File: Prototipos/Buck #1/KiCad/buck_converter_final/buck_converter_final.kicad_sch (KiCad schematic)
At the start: 25 parts, among them J1 Conn_01x03_Pin, J2 Screw_Terminal_01x02, J3 Screw_Terminal_01x02, Q1 IRF9540NPBF, Q3 NPN

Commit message: Primera versión PCB final Buck
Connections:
- net AGND: now also J1.2 (Pin_2); no longer J1.3 (Pin_3)
- net RETRO_MICRO: now also J1.3 (Pin_3); no longer J1.2 (Pin_2)
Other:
- company: (none) -> Alesandria - Cignetti - Galliano
- title: (none) -> PCB final Convertidor Buck
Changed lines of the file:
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@@
 	(generator_version "9.0")
 	(paper "A4")
+	(title_block
+		(title "PCB final Convertidor Buck")
+		(company "Alesandria - Cignetti - Galliano")
+	)
 	(rectangle
 		(start 130.81 85.09)
@@
 	(wire
 		(pts
+			(xy 81.28 38.1) (xy 101.6 38.1)
+		)
+		(stroke
+			(width 0)
+			(type default)
+		)
+	)
+	(wire
+		(pts
 			(xy 102.87 81.28) (xy 133.35 81.28)
 		)
@@
 	(wire
 		(pts
-			(xy 81.28 38.1) (xy 83.82 38.1)
-		)
-		(stroke
-			(width 0)
-			(type default)
-		)
-	)
-	(wire
-		(pts
 			(xy 133.35 81.28) (xy 149.86 81.28)
 		)
@@
 	(wire
 		(pts
-			(xy 81.28 40.64) (xy 83.82 40.64)
-		)
-		(stroke
-			(width 0)
-			(type default)
-		)
-	)
-	(wire
-		(pts
 			(xy 138.43 64.77) (xy 138.43 69.85)
 		)
@@
 	(wire
 		(pts
+			(xy 83.82 40.64) (xy 81.28 40.64)
+		)
+		(stroke
+			(width 0)
+			(type default)
+		)
+	)
+	(wire
+		(pts
 			(xy 118.11 41.91) (xy 123.19 41.91)
 		)
@@
 	(wire
 		(pts
-			(xy 83.82 40.64) (xy 83.82 41.91)
-		)
-		(stroke
-			(width 0)
-			(type default)
-		)
-	)
-	(wire
-		(pts
 			(xy 156.21 87.63) (xy 156.21 90.17)
 		)
@@
 		(pts
 			(xy 181.61 96.52) (xy 181.61 95.25)
+		)
+		(stroke
+			(width 0)
+			(type default)
+		)
+	)
+	(wire
+		(pts
+			(xy 101.6 38.1) (xy 101.6 39.37)
 		)
 		(stroke
@@
 	(global_label "RETRO_MICRO"
 		(shape input)
-		(at 83.82 38.1 0)
+		(at 83.82 40.64 0)
 		(fields_autoplaced yes)
 		(effects
@@
 		)
 		(property "Intersheetrefs" "${INTERSHEET_REFS}"
-			(at 99.6866 38.1 0)
+			(at 99.6866 40.64 0)
 			(effects
 				(font
@@
 	(symbol
 		(lib_id "power:GND")
-		(at 83.82 41.91 0)
+		(at 101.6 39.37 0)
 		(unit 1)
 		(exclude_from_sim no)
@@
 		(dnp no)
 		(property "Reference" "#PWR01"
-			(at 83.82 48.26 0)
+			(at 101.6 45.72 0)
 			(effects
 				(font
@@
 		)
 		(property "Value" "AGND"
-			(at 83.82 45.466 0)
+			(at 101.6 42.926 0)
 			(effects
 				(font
@@
 		)
 		(property "Footprint" ""
-			(at 83.82 41.91 0)
+			(at 101.6 39.37 0)
 			(effects
 				(font
@@
 		)
 		(property "Datasheet" ""
-			(at 83.82 41.91 0)
+			(at 101.6 39.37 0)
 			(effects
 				(font
@@
 		)
 		(property "Description" "Power symbol creates a global label with name \"GND\" , ground"
-			(at 83.82 41.91 0)
-			(effects
-				(font
+			(at 101.6 39.37 0)
+			(effects
+				(font

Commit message: Mejoras en PCB
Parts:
- R11: value 33k -> 2.2k
- R13: value 1k -> 100k
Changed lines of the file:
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@@
 			)
 		)
-		(property "Value" "1k"
+		(property "Value" "100k"
 			(at 158.242 111.76 0)
 			(effects
@@
 			)
 		)
-		(property "Value" "33k"
+		(property "Value" "2.2k"
 			(at 152.4 105.918 90)
 			(effects

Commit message: Avances PCB convertidor Buck
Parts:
- removed J1: Conn_01x03_Pin, Connector_PinHeader_2.54mm:PinHeader_1x03_P2.54mm_Vertical, symbol Connector:Conn_01x03_Pin
- removed J2: Screw_Terminal_01x02, TerminalBlock_Phoenix:TerminalBlock_Phoenix_MKDS-1,5-2-5.08_1x02_P5.08mm_Horizontal, symbol Connector:Screw_Terminal_01x02
- added J4: ~, Proyecto_Final:BUS_PCIE_x4_NSH, symbol Proyecto_Final:PCIE_x4_NSH
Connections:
- net 12V: now also J4.4 (12Vdc)
- net AGND: now also J4.40 (AGND)
- net PGND: now also J4.2 (PGND)
- net PWM_CONTROL: now also J4.8 (S2)
- net RETRO_MICRO: now also J4.10 (S4)

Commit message: Avances en PCB final buck, versión 1.1
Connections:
- net PWM_CONTROL: now also J4.26 (S20); no longer J4.8 (S2)
- net RETRO_MICRO: now also J4.8 (S2); no longer J4.10 (S4)
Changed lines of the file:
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@@
+	(wire
+		(pts
+			(xy 257.81 71.12) (xy 254 71.12)
+		)
+		(stroke
+			(width 0)
+			(type default)
+		)
+	)
 	(wire
 		(pts
@@
 	(wire
 		(pts
-			(xy 254 50.8) (xy 256.54 50.8)
-		)
-		(stroke
-			(width 0)
-			(type default)
-		)
-	)
-	(wire
-		(pts
 			(xy 149.86 71.12) (xy 149.86 81.28)
 		)
@@
 	(wire
 		(pts
-			(xy 254 48.26) (xy 256.54 48.26)
-		)
-		(stroke
-			(width 0)
-			(type default)
-		)
-	)
-	(wire
-		(pts
 			(xy 167.64 88.9) (xy 166.37 88.9)
+		)
+		(stroke
+			(width 0)
+			(type default)
+		)
+	)
+	(wire
+		(pts
+			(xy 256.54 48.26) (xy 254 48.26)
 		)
 		(stroke
@@
 	(global_label "PWM_CONTROL"
 		(shape output)
-		(at 256.54 48.26 0)
+		(at 257.81 71.12 0)
 		(fields_autoplaced yes)
 		(effects
@@
 		)
 		(property "Intersheetrefs" "${INTERSHEET_REFS}"
-			(at 273.1928 48.26 0)
+			(at 274.4628 71.12 0)
 			(effects
 				(font
@@
 	(global_label "RETRO_MICRO"
 		(shape input)
-		(at 256.54 50.8 0)
+		(at 256.54 48.26 0)
 		(fields_autoplaced yes)
 		(effects
@@
 		)
 		(property "Intersheetrefs" "${INTERSHEET_REFS}"
-			(at 272.4066 50.8 0)
-			(effects
-				(font
+			(at 272.4066 48.26 0)
+			(effects
+				(font

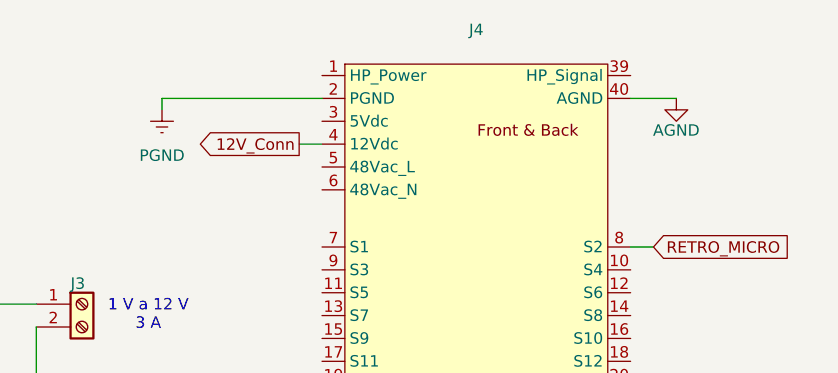
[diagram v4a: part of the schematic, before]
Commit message: Agregado pin HP
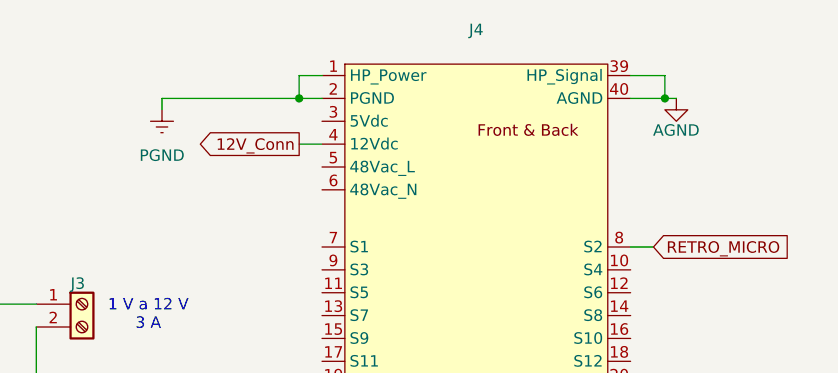
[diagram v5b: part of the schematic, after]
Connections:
- net AGND: now also J4.39 (HP_Signal)
- net PGND: now also J4.1 (HP_Power)
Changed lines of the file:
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@@
+	)
+	(junction
+		(at 257.81 31.75)
+		(diameter 0)
+		(color 0 0 0 0)
 	)
 	(junction
@@
 	)
 	(junction
+		(at 217.17 31.75)
+		(diameter 0)
+		(color 0 0 0 0)
+	)
+	(junction
 		(at 133.35 74.93)
 		(diameter 0)
@@
 	(wire
 		(pts
+			(xy 257.81 29.21) (xy 257.81 31.75)
+		)
+		(stroke
+			(width 0)
+			(type default)
+		)
+	)
+	(wire
+		(pts
 			(xy 100.33 54.61) (xy 105.41 54.61)
 		)
@@
 	(wire
 		(pts
-			(xy 201.93 31.75) (xy 219.71 31.75)
+			(xy 201.93 31.75) (xy 217.17 31.75)
 		)
 		(stroke
@@
 	(wire
 		(pts
+			(xy 219.71 29.21) (xy 217.17 29.21)
+		)
+		(stroke
+			(width 0)
+			(type default)
+		)
+	)
+	(wire
+		(pts
 			(xy 133.35 74.93) (xy 133.35 81.28)
 		)
@@
 	(wire
 		(pts
-			(xy 254 31.75) (xy 259.08 31.75)
+			(xy 254 31.75) (xy 257.81 31.75)
 		)
 		(stroke
@@
 	(wire
 		(pts
+			(xy 254 29.21) (xy 257.81 29.21)
+		)
+		(stroke
+			(width 0)
+			(type default)
+		)
+	)
+	(wire
+		(pts
 			(xy 111.76 41.91) (xy 111.76 45.72)
 		)
@@
 	(wire
 		(pts
+			(xy 217.17 29.21) (xy 217.17 31.75)
+		)
+		(stroke
+			(width 0)
+			(type default)
+		)
+	)
+	(wire
+		(pts
 			(xy 166.37 96.52) (xy 166.37 99.06)
 		)
@@
 		)
 		(stroke
+			(width 0)
+			(type default)
+		)
+	)
+	(wire
+		(pts
+			(xy 217.17 31.75) (xy 219.71 31.75)
+		)
+		(stroke
+			(width 0)
+			(type default)
+		)
+	)
+	(wire
+		(pts
+			(xy 257.81 31.75) (xy 259.08 31.75)
+		)
+		(stroke

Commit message: Reestructuración de esquemático y PCB
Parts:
- removed J4: ~, Proyecto_Final:BUS_PCIE_x4_NSH, symbol Proyecto_Final:PCIE_x4_NSH
- added D4: D_Small, Diode_THT:D_DO-41_SOD81_P7.62mm_Horizontal, symbol Device:D_Small
- added J1: ~, Proyecto_final:BUS_PCIE_x4_NSH, symbol Proyecto_Final:PCIE_x4_NSH
- added J3: Screw_Terminal_01x02, TerminalBlock_Phoenix:TerminalBlock_Phoenix_MKDS-1,5-2-5.08_1x02_P5.08mm_Horizontal, symbol Connector:Screw_Terminal_01x02
- added K1: SANYOU_SRD_Form_C, Relay_THT:Relay_SPDT_SANYOU_SRD_Series_Form_C, symbol Relay:SANYOU_SRD_Form_C
- added Q3: BC548, Package_TO_SOT_THT:TO-92_Inline_Wide, symbol Transistor_BJT:BC548
- added R13: 12k, Resistor_THT:R_Axial_DIN0207_L6.3mm_D2.5mm_P7.62mm_Horizontal, symbol Device:R_Small
- added R7: 10k, Resistor_THT:R_Axial_DIN0207_L6.3mm_D2.5mm_P7.62mm_Horizontal, symbol Device:R_Small
- added R8: 15k, Resistor_THT:R_Axial_DIN0207_L6.3mm_D2.5mm_P7.62mm_Horizontal, symbol Device:R_Small
- renumbered C7 to C2, C2 to C3, C3 to C4, D4 to D1, D1 to D2, D2 to D3, J3 to J2, Q3 to Q1, Q1 to Q2, R11 to R1, R8 to R10, R9 to R11, R10 to R12, R12 to R2, R13 to R3, R2 to R4, R14 to R5, R5 to R6, R7 to R9
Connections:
- net 12V: now also J1.4 (12Vdc)
- net AGND: now also J1.26 (HP_Signal), J1.7 (AGND), Q3.3 (E), R8.2
- net PGND: now also J1.1 (HP_Power), J1.2 (PGND), J3.2 (Pin_2)
- net PWM_CONTROL: now also J1.11 (S3)
- net RETRO_MICRO: now also J1.10 (S2)
- net at C5.1, L1.2, R9.1: now also K1.1; no longer J2.1 (Pin_1)
- net Gate renamed GATE
- new net: Q3.2 (B), R13.2
- new net 3.3Vcc: J1.8 (3,3Vdc_Signal), R7.1
- new net 5Vdc: D4.1 (K), J1.3 (5Vdc), K1.5
- new net IDENT_V: J1.25 (MODULE_IDENT), R7.2, R8.1
- new net INDUCTIVE_LOAD: J3.1 (Pin_1), K1.3
- new net RELAY_T2: D4.2 (A), K1.2, Q3.1 (C)
- new net RESISTIVE_LOAD: J2.1 (Pin_1), K1.4
- new net UC_RELAY: J1.9 (S1), R13.1
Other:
- note added: "Identification Circuit"
- note added: "MOSFET-p driver with BJT"
- note added: "Relay Driver"
- note removed: "Disparar MOSFET-p con BJT"
- note removed: "Puede que sea innecesario el capacitor de acople de masas"
- moved on the sheet: C1, C2, C3, C4, C5, C6, D1, D2, D3, J2, L1, Q1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

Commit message: Avances en PCB buck
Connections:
- net PWM_CONTROL: now also J1.9 (S1); no longer J1.11 (S3)
- net RETRO_MICRO: now also J1.11 (S3); no longer J1.10 (S2)
- net UC_RELAY: now also J1.10 (S2); no longer J1.9 (S1)
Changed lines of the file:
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@@
+	(wire
+		(pts
+			(xy 35.56 54.61) (xy 38.1 54.61)
+		)
+		(stroke
+			(width 0)
+			(type default)
+		)
+	)
 	(wire
 		(pts
@@
 	(wire
 		(pts
+			(xy 35.56 52.07) (xy 38.1 52.07)
+		)
+		(stroke
+			(width 0)
+			(type default)
+		)
+	)
+	(wire
+		(pts
 			(xy 158.75 97.79) (xy 158.75 101.6)
 		)
@@
 	(wire
 		(pts
-			(xy 35.56 52.07) (xy 38.1 52.07)
-		)
-		(stroke
-			(width 0)
-			(type default)
-		)
-	)
-	(wire
-		(pts
 			(xy 186.69 67.31) (xy 184.15 67.31)
 		)
@@
 		(pts
 			(xy 49.53 87.63) (xy 50.8 87.63)
-		)
-		(stroke
-			(width 0)
-			(type default)
-		)
-	)
-	(wire
-		(pts
-			(xy 35.56 54.61) (xy 38.1 54.61)
 		)
 		(stroke
@@
 	(global_label "RETRO_MICRO"
 		(shape input)
-		(at 35.56 54.61 180)
-		(fields_autoplaced yes)
-		(effects
-			(font
-				(size 1.27 1.27)
-			)
-			(justify right)
-		)
-		(property "Intersheetrefs" "${INTERSHEET_REFS}"
-			(at 19.6934 54.61 0)
+		(at 35.56 57.15 180)
+		(fields_autoplaced yes)
+		(effects
+			(font
+				(size 1.27 1.27)
+			)
+			(justify right)
+		)
+		(property "Intersheetrefs" "${INTERSHEET_REFS}"
+			(at 19.6934 57.15 0)
 			(effects
 				(font
@@
 	(global_label "PWM_CONTROL"
 		(shape output)
-		(at 35.56 57.15 180)
-		(fields_autoplaced yes)
-		(effects
-			(font
-				(size 1.27 1.27)
-			)
-			(justify right)
-		)
-		(property "Intersheetrefs" "${INTERSHEET_REFS}"
-			(at 18.9072 57.15 0)
+		(at 35.56 52.07 180)
+		(fields_autoplaced yes)
+		(effects
+			(font
+				(size 1.27 1.27)
+			)
+			(justify right)
+		)
+		(property "Intersheetrefs" "${INTERSHEET_REFS}"
+			(at 18.9072 52.07 0)
 			(effects
 				(font
@@
 	(global_label "UC_RELAY"
 		(shape output)
-		(at 35.56 52.07 180)
-		(fields_autoplaced yes)
-		(effects
-			(font
-				(size 1.27 1.27)
-			)
-			(justify right)
-		)
-		(property "Intersheetrefs" "${INTERSHEET_REFS}"
-			(at 23.3824 52.07 0)
-			(effects
-				(font
+		(at 35.56 54.61 180)
+		(fields_autoplaced yes)
+		(effects
+			(font
+				(size 1.27 1.27)
+			)
+			(justify right)
+		)
+		(property "Intersheetrefs" "${INTERSHEET_REFS}"
+			(at 23.3824 54.61 0)
+			(effects
+				(font

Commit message: Avances en PCB, etiqueta de bloques
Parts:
- Q2: footprint KiCad-Libraries:TO254P470X1000X2000-3P -> Package_TO_SOT_THT:TO-220-3_Horizontal_TabDown
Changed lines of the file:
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@@
 			)
 		)
-		(property "Footprint" "KiCad-Libraries:TO254P470X1000X2000-3P"
+		(property "Footprint" "Package_TO_SOT_THT:TO-220-3_Horizontal_TabDown"
 			(at 134.62 50.8 0)
 			(effects
